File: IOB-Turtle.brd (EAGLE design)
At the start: 53.3 x 20.3 mm, 12 parts, among them J1 RJ12/6

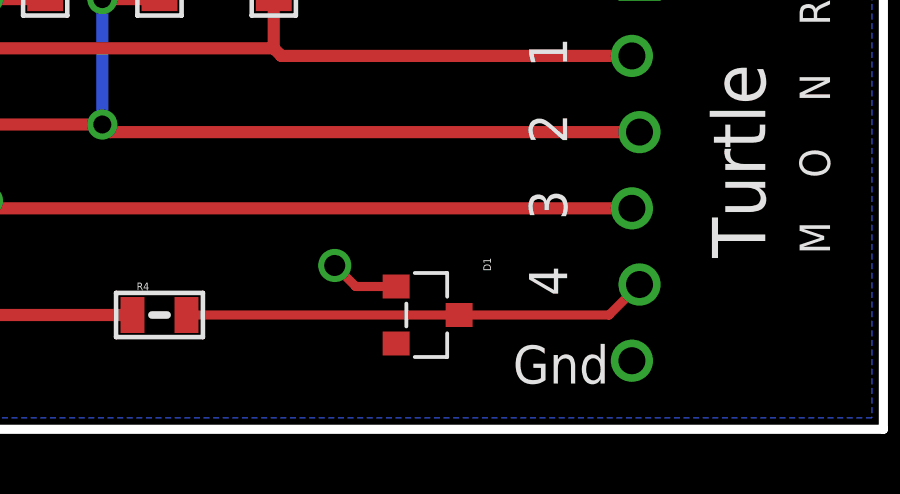
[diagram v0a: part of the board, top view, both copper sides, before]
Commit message: fixed SPCoast.lbr orientation
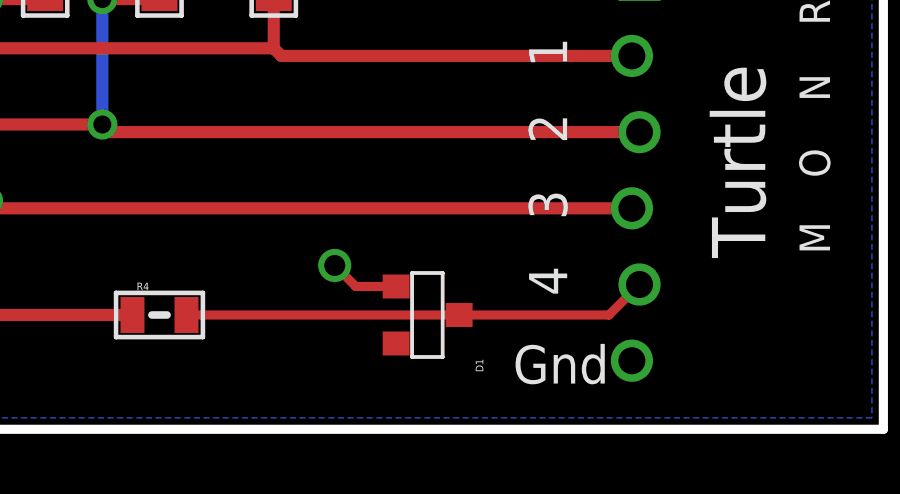
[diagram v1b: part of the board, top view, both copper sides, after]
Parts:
- turned D1 to 180 degrees
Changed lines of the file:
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@@
 <layer number="60" name="bCarbon" color="7" fill="1" visible="no" active="no"/>
 <layer number="90" name="Modules" color="5" fill="1" visible="no" active="no"/>
+<layer number="100" name="Muster" color="7" fill="1" visible="no" active="no"/>
+<layer number="101" name="Hidden" color="57" fill="4" visible="yes" active="yes"/>
+<layer number="102" name="Changes" color="13" fill="1" visible="yes" active="yes"/>
+<layer number="103" name="tMap" color="29" fill="4" visible="yes" active="yes"/>
+<layer number="104" name="Name" color="16" fill="1" visible="yes" active="yes"/>
+<layer number="105" name="tPlate" color="7" fill="1" visible="yes" active="yes"/>
+<layer number="106" name="bPlate" color="7" fill="1" visible="yes" active="yes"/>
+<layer number="107" name="Crop" color="7" fill="1" visible="yes" active="yes"/>
+<layer number="108" name="fp8" color="7" fill="1" visible="yes" active="yes"/>
+<layer number="109" name="fp9" color="7" fill="1" visible="yes" active="yes"/>
+<layer number="110" name="fp0" color="7" fill="1" visible="yes" active="yes"/>
+<layer number="111" name="bdokum" color="7" fill="1" visible="yes" active="yes"/>
+<layer number="112" name="tSilk" color="7" fill="1" visible="no" active="no"/>
+<layer number="113" name="IDFDebug" color="7" fill="1" visible="yes" active="yes"/>
+<layer number="114" name="Rect_Pads" color="7" fill="1" visible="yes" active="yes"/>
+<layer number="115" name="_tsilk" color="7" fill="1" visible="yes" active="yes"/>
+<layer number="116" name="Patch_BOT" color="9" fill="4" visible="yes" active="yes"/>
+<layer number="117" name="tTestmark" color="7" fill="1" visible="yes" active="yes"/>
+<layer number="118" name="Rect_Pads" color="7" fill="1" visible="no" active="no"/>
+<layer number="119" name="_tNames" color="7" fill="1" visible="yes" active="yes"/>
+<layer number="120" name="_bNames" color="7" fill="1" visible="yes" active="yes"/>
+<layer number="121" name="_tsilk" color="7" fill="1" visible="yes" active="yes"/>
+<layer number="122" name="_bsilk" color="7" fill="1" visible="yes" active="yes"/>
+<layer number="123" name="tTestmark" color="7" fill="1" visible="yes" active="yes"/>
+<layer number="124" name="bTestmark" color="7" fill="1" visible="yes" active="yes"/>
 <layer number="125" name="_tNames" color="14" fill="1" visible="no" active="yes"/>
+<layer number="126" name="_bNames" color="7" fill="1" visible="yes" active="yes"/>
+<layer number="127" name="_tValues" color="7" fill="1" visible="no" active="no"/>
+<layer number="128" name="_bValues" color="7" fill="1" visible="no" active="no"/>
+<layer number="129" name="Mask" color="7" fill="1" visible="yes" active="yes"/>
+<layer number="130" name="SMDSTROOK" color="7" fill="1" visible="yes" active="yes"/>
+<layer number="131" name="tAdjust" color="7" fill="1" visible="yes" active="yes"/>
+<layer number="132" name="bAdjust" color="7" fill="1" visible="yes" active="yes"/>
+<layer number="144" name="Drill_legend" color="7" fill="1" visible="yes" active="yes"/>
+<layer number="146" name="Housing" color="7" fill="1" visible="yes" active="yes"/>
+<layer number="147" name="Edge" color="7" fill="1" visible="yes" active="yes"/>
+<layer number="148" name="ReferenceLC" color="7" fill="1" visible="yes" active="yes"/>
+<layer number="149" name="ReferenceLS" color="7" fill="1" visible="yes" active="yes"/>
+<layer number="150" name="Notes" color="7" fill="1" visible="yes" active="yes"/>
+<layer number="151" name="HeatSink" color="7" fill="1" visible="yes" active="yes"/>
+<layer number="152" name="_bDocu" color="7" fill="1" visible="no" active="no"/>
+<layer number="153" name="FabDoc1" color="7" fill="1" visible="yes" active="yes"/>
+<layer number="154" name="FabDoc2" color="7" fill="1" visible="yes" active="yes"/>
+<layer number="155" name="FabDoc3" color="7" fill="1" visible="yes" active="yes"/>
+<layer number="199" name="Contour" color="7" fill="1" visible="yes" active="yes"/>
+<layer number="200" name="200bmp" color="1" fill="10" visible="yes" active="yes"/>
+<layer number="201" name="201bmp" color="2" fill="10" visible="yes" active="yes"/>
+<layer number="202" name="202bmp" color="3" fill="10" visible="yes" active="yes"/>
+<layer number="203" name="203bmp" color="4" fill="10" visible="yes" active="yes"/>
+<layer number="204" name="204bmp" color="5" fill="10" visible="yes" active="yes"/>
+<layer number="205" name="205bmp" color="6" fill="10" visible="yes" active="yes"/>
+<layer number="206" name="206bmp" color="7" fill="10" visible="yes" active="yes"/>
+<layer number="207" name="207bmp" color="8" fill="10" visible="yes" active="yes"/>
+<layer number="208" name="208bmp" color="9" fill="10" visible="yes" active="yes"/>
+<layer number="209" name="209bmp" color="7" fill="1" visible="yes" active="yes"/>
+<layer number="210" name="210bmp" color="7" fill="1" visible="yes" active="yes"/>
+<layer number="211" name="211bmp" color="12" fill="1" visible="no" active="no"/>
+<layer number="212" name="212bmp" color="13" fill="1" visible="no" active="no"/>
+<layer number="213" name="213bmp" color="14" fill="1" visible="no" active="no"/>
+<layer number="214" name="214bmp" color="15" fill="1" visible="no" active="no"/>
+<layer number="215" name="215bmp" color="16" fill="1" visible="no" active="no"/>
+<layer number="216" name="216bmp" color="17" fill="1" visible="no" active="no"/>
+<layer number="217" name="217bmp" color="18" fill="1" visible="no" active="no"/>
+<layer number="218" name="218bmp" color="19" fill="1" visible="no" active="no"/>
+<layer number="219" name="219bmp" color="20" fill="1" visible="no" active="no"/>
+<layer number="220" name="220bmp" color="21" fill="1" visible="no" active="no"/>
+<layer number="221" name="221bmp" color="22" fill="1" visible="no" active="no"/>
+<layer number="222" name="222bmp" color="23" fill="1" visible="no" active="no"/>
+<layer number="223" name="223bmp" color="24" fill="1" visible="no" active="no"/>
+<layer number="224" name="224bmp" color="25" fill="1" visible="no" active="no"/>
+<layer number="225" name="225bmp" color="7" fill="1" visible="yes" active="yes"/>
+<layer number="226" name="226bmp" color="7" fill="1" visible="yes" active="yes"/>
+<layer number="227" name="227bmp" color="7" fill="1" visible="yes" active="yes"/>
+<layer number="228" name="228bmp" color="7" fill="1" visible="yes" active="yes"/>
+<layer number="229" name="229bmp" color="7" fill="1" visible="yes" active="yes"/>
+<layer number="230" name="230bmp" color="7" fill="1" visible="yes" active="yes"/>
+<layer number="231" name="231bmp" color="7" fill="1" visible="yes" active="yes"/>
+<layer number="232" name="Eagle3D_PG2" color="7" fill="1" visible="yes" active="yes"/>
+<layer number="233" name="Eagle3D_PG3" color="7" fill="1" visible="yes" active="yes"/>
+<layer number="247" name="wrappinf" color="7" fill="1" visible="yes" active="yes"/>
+<layer number="248" name="Housing" color="7" fill="1" visible="no" active="no"/>
+<layer number="249" name="Edge" color="7" fill="1" visible="no" active="no"/>
+<layer number="250" name="Descript" color="3" fill="1" visible="no" active="no"/>
+<layer number="251" name="SMDround" color="12" fill="11" visible="no" active="no"/>
+<layer number="252" name="BR-BS" color="7" fill="1" visible="yes" active="yes"/>
+<layer number="253" name="BR-LS" color="7" fill="1" visible="yes" active="yes"/>
+<layer number="254" name="cooling" color="7" fill="1" visible="yes" active="yes"/>
+<layer number="255" name="routoute" color="7" fill="1" visible="yes" active="yes"/>
 </layers>
 <board>
@@
 <element name="FID1" library="SPCoast" package="FIDUCIAL_1MM" value="FIDUCIAL" x="15.875" y="1.27" smashed="yes"/>
 <element name="FID2" library="SPCoast" package="FIDUCIAL_1MM" value="FIDUCIAL" x="51.435" y="18.415" smashed="yes"/>
-<element name="D1" library="SPCoast" package="SOT23-3" value="4.7v" x="38.1" y="3.81" smashed="yes" rot="R270">
-<attribute name="NAME" x="40.005" y="5.715" size="0.254" layer="25" rot="R270"/>
-<attribute name="VALUE" x="36.957" y="1.143" size="0.8128" layer="27"/>
+<element name="D1" library="SPCoast" package="SOT23-3" value="4.7v" x="38.1" y="3.81" smashed="yes" rot="R180">
+<attribute name="NAME" x="40.005" y="1.905" size="0.254" layer="25" rot="R90"/>
+<attribute name="VALUE" x="35.433" y="4.953" size="0.8128" layer="27" rot="R270"/>
 </element>
 <element name="R4" library="SPCoast" package="0805-RES" value="1k0" x="29.21" y="3.81" smashed="yes">

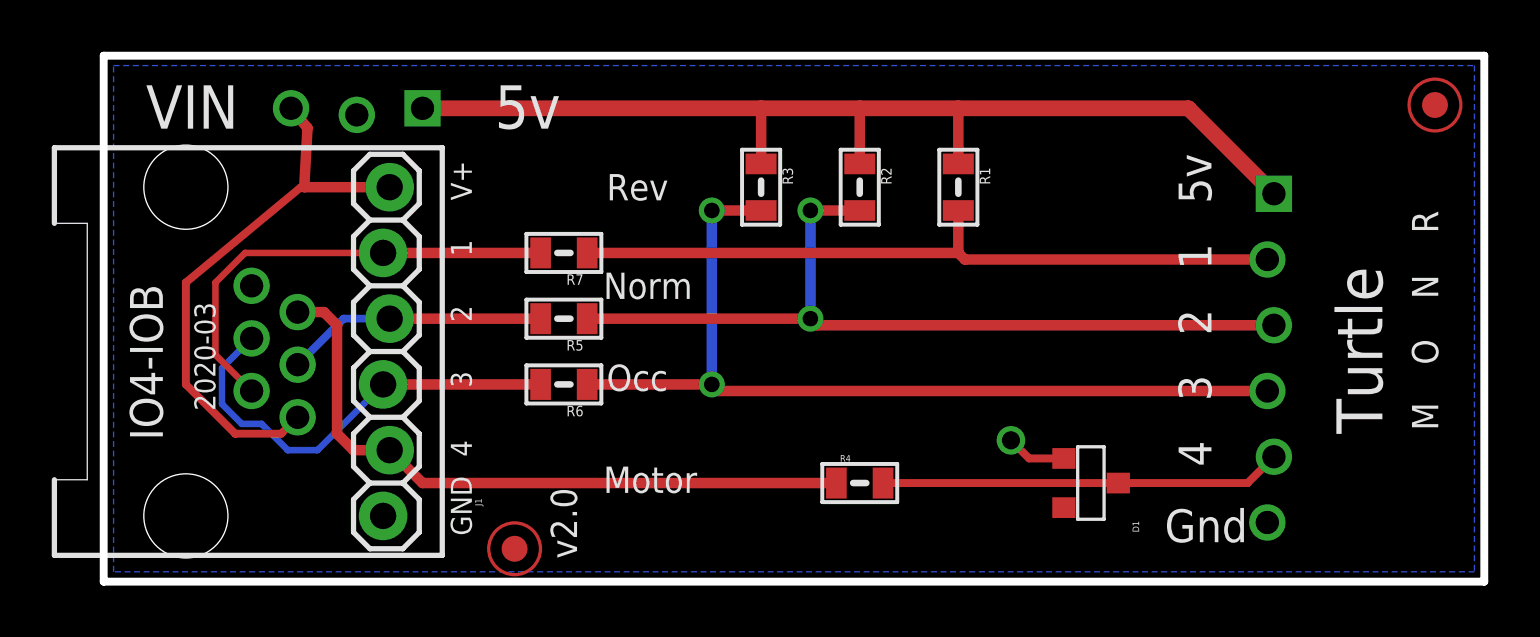
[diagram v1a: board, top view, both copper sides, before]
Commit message: add lpf on inputs, normalized silkscreen layout across IOBs
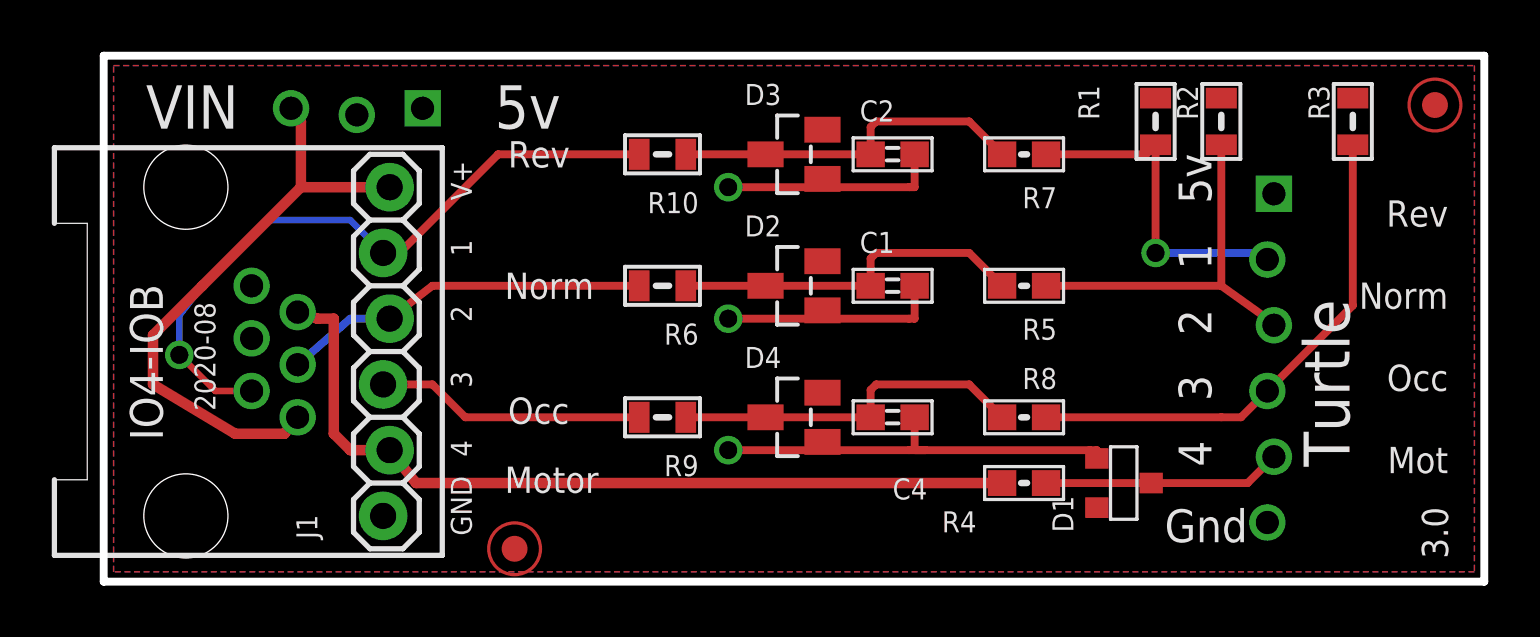
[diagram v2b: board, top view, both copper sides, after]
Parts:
- added C1, C2, C4: 0.01uF, SPCoast:0603-CAP
- added D2, D3, D4: BAT54S, SPCoast:SOT23
- added R10, R9: 82R, SPCoast:0805-RES
- added R8: 1K0, SPCoast:0603-RES
- R4: value 1k0 -> 1K0; device SPCoast:0805-RES -> SPCoast:0603-RES
- R5, R7: value 200R -> 1K0; device SPCoast:0805-RES -> SPCoast:0603-RES
- R6: value 200R -> 82R
- moved R3 23.0 mm to (48.3, 17.8)
- moved R7 18.2 mm to (35.6, 16.5)
- moved R5 17.8 mm to (35.6, 11.4)
- moved R2 14.2 mm to (43.2, 17.8)
- moved R1 8.03 mm to (40.6, 17.8)
- moved R4 6.35 mm to (35.6, 3.81)
- moved R6 5.39 mm to (21.6, 11.4)
- moved D1 1.27 mm to (39.4, 3.81)
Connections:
- removed net IO4-4: J1.4, J1.4@1, R6.2
- new net N$1: J1.4, J1.4@1, R9.2
- new net N$14: C4.1, D4.3, R8.2, R9.1
- new net N$2: C1.1, D2.3, R5.2, R6.1
- new net N$3: C2.1, D3.3, R10.1, R7.2
- net !OCC: now also R8.1; no longer R6.1
- net GND: now also C1.2, C2.2, C4.2, D2.1, D3.1, D4.1
- net IO4-2: now also R10.2; no longer R7.2
- net IO4-3: now also R6.2; no longer R5.2
- net VCC: now also D2.2, D3.2, D4.2
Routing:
- net VCC: track 40.7 -> 0.00 mm
- net GND: track 2.34 -> 35.0 mm, vias 1 -> 3
- net !NORM: track 32.7 -> 14.8 mm, vias 2 -> 0
- net IO4-4: track 17.1 -> 0.00 mm
- net !OCC: track 35.0 -> 19.9 mm, vias 2 -> 0
- net !REV: track 28.0 -> 13.0 mm, vias 0 -> 1
- net N$3: track 0.00 -> 13.9 mm
- net N$2: track 0.00 -> 13.9 mm
- net N$14: track 0.00 -> 13.9 mm
- net N$1: track 0.00 -> 10.4 mm
- net IO4-2: track 17.8 -> 26.4 mm, vias 0 -> 1
- net IO4-5: track 26.0 -> 32.6 mm
- net P4: track 15.5 -> 9.22 mm
- net IO4-3: track 10.1 -> 14.3 mm
- net VCCIO: track 21.8 -> 23.0 mm
- added copper zone on layer 1, net VCC
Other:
- board text added: "2020-08"
- board text added: "3.0"
- board text added: "C1"
- board text added: "C2"
- board text added: "C4"
- board text added: "D2"
- board text added: "D3"
- board text added: "D4"
- board text added: "Green Header"
- board text added: "Mot"
- board text added: "R10"
- board text added: "R8"
- board text added: "R9"
- board text removed: "2020-03"
- board text removed: "M"
- board text removed: "N"
- board text removed: "O"
- board text removed: "R"
- board text removed: "v2.0"
